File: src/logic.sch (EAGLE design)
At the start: 70 parts, among them CON1 CON-4P-TABS-JST_GH-RA, CON11 PINHEAD_1X04-2, CON12 PINHEAD_1X04-2, CON2 PINHEAD_1X04-2.54, CON3 PINHEAD_2X04-PLS-2, CON4 PINHEAD_2X03-PTH-2, CON5 PINHEAD_2X03-PTH-2, IC1 STM32F105RCT6, IC10 LM75-TSSOP8, IC11 LM75-TSSOP8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

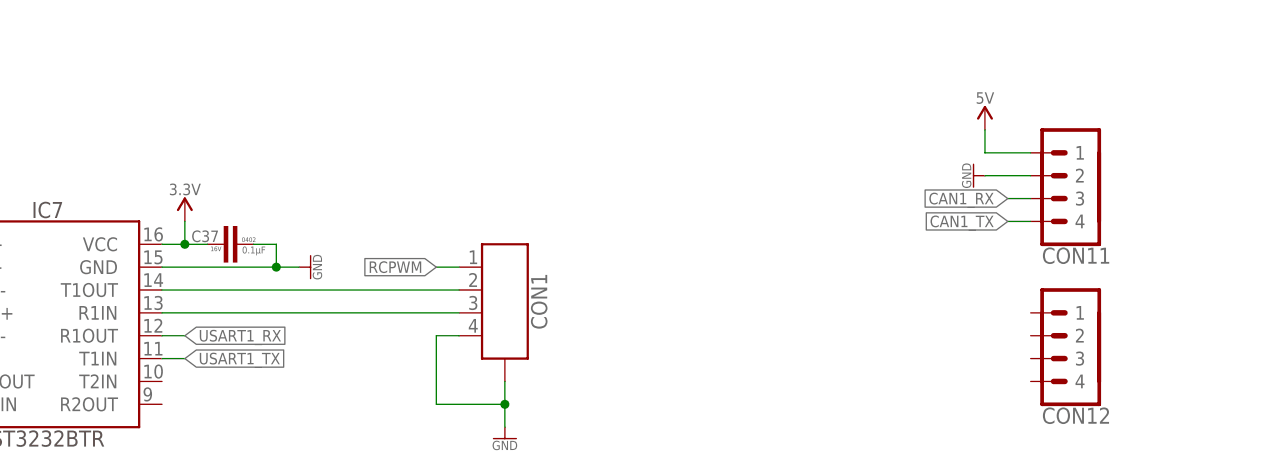
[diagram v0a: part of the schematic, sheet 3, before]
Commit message: RC PWM updated
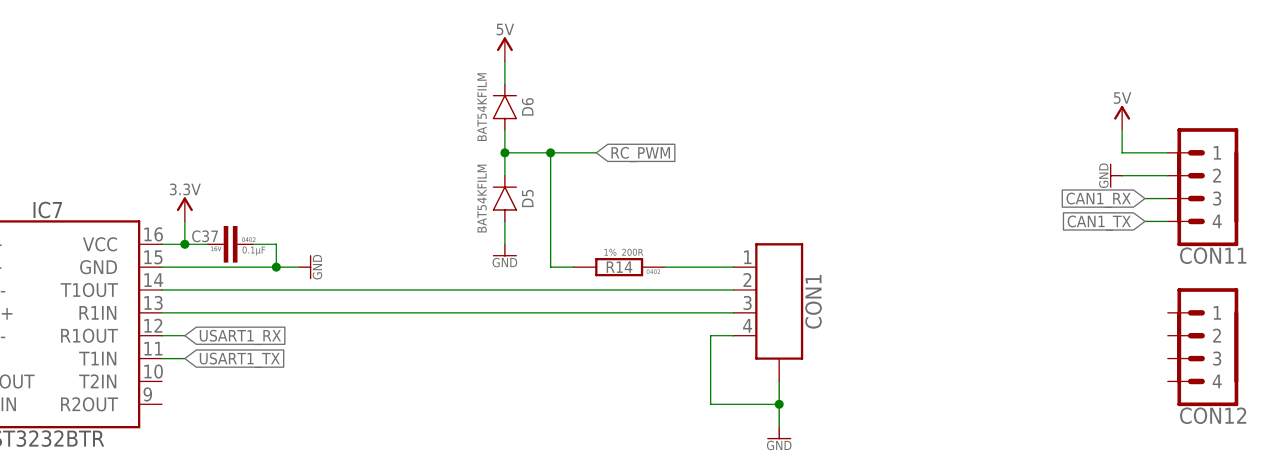
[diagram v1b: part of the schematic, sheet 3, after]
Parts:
- added D5, D6: BAT54KFILM, Diodes:BAT54KFILM
- added R14: 200R, rc:R-1%-0402
- C1, C31: value 18pF -> 9pF; AEC-Q --- -> (none); DIGIKEY# 399-8828-1-ND -> 1276-1617-1-ND; LCSC# (none) -> C111805; MANF Kemet -> Samsung Electro-Mechanics; MANF# CBR04C180F5GAC -> CL05C090DB5NNNC
- C15, C22, C25, C30: value 5600pF -> 4700pF; DIGIKEY# 1276-1579-1-ND -> 1276-1125-1-ND; LCSC# (none) -> C1538; MANF# CL05B562KB5NNNC -> CL05B472KB5NNNC
- IC2: LCSC# (none) -> C81340
- R10, R8: value 47K -> 51K; DIGIKEY# 311-47.0KCRCT-ND -> 13-RT0805FRE0751KLCT-ND; LCSC# (none) -> C25794; MANF# RC0805FR-0747KL -> RT0805FRE0751KL; OPERATING_TEMP -55°C ~ 155°C -> -55°C ~ 155°C
- R11, R15, R9: value 1K5 -> 1K8; DIGIKEY# 311-1.50KLRCT-ND -> 311-1.80KLRCT-ND; LCSC# (none) -> C25871; MANF# RC0402FR-071K5L -> RC0402FR-071K8L
- R7: value 47K -> 51K; DIGIKEY# 311-47.0KCRCT-ND -> 13-RT0805FRE0751KLCT-ND; LCSC# (none) -> C25794; MANF# RC0805FR-0747KL -> RT0805FRE0751KL
- X1: DIGIKEY# 1253-1198-1-ND -> (none); ESR (none) -> 60Ω; LOAD_CAPACITANCE (none) -> 9pF; LSCSC# (none) -> C13738; MANF (none) -> Yangxing Tech; MANF# CX3225GB24000P0HPQCC -> X322516MLB4SI
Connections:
- removed net RCPWM: CON1.1
- removed net TSENS_OS: IC1.PB4
- net GND: now also D5.A
- net N$2: now also CON1.1, R14.1
- net RC_PWM: now also D5.C, D6.A, R14.2
- net VDD_5V: now also D6.C
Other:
- note added: "Max PHASE_x voltage should be around VDC_max VDC_max = 22 * 4.2 V = 92.4 V With resistor divider formed by 51K and 1K8 resistors SENSE_x max voltage is 92.4 * (1.8/(51+1.8)) = 3.15 V"
- note removed: "Max PHASE_x voltage should be around VDC_max VDC_max = 22 * 4.2 V = 92.4 V With resistor divider formed by 47K and 1K5 resistors SENSE_x max voltage is 92.4 * (1.5/(47+1.5)) = 2.85 V"
- note removed: "Place R26 TO WRITE PROTECT"
- moved on the sheet: C1, C31, CON1, CON11, CON12

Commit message: Crystal attributes update
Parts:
- X1: DIGIKEY# (none) -> SER4372CT-ND; MANF Yangxing Tech -> EPSON; MANF# X322516MLB4SI -> TSX-3225 16.0000MF18X-AC6
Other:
- note added: "Vout = 1.225 * (10/1 + 1) ~13.5 V"
- note added: "Vout = 1.225 * (Rfb2/Rfb1 + 1)"
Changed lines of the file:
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@@
 <attribute name="MANF#" value="RC0402FR-0714KL"/>
 </part>
-<part name="RFB2" library="rc" library_urn="urn:adsk.eagle:library:2539423" deviceset="R" device="-0402" package3d_urn="urn:adsk.eagle:package:2539456/2" technology="-1%" value="3K">
-<attribute name="DIGIKEY#" value="311-3.0KJRCT-ND"/>
-<attribute name="MANF" value="Yageo"/>
-<attribute name="MANF#" value="RC0402JR-073KL"/>
+<part name="RFB2" library="rc" library_urn="urn:adsk.eagle:library:2539423" deviceset="R" device="-0402" package3d_urn="urn:adsk.eagle:package:2539456/2" technology="-1%" value="10K">
+<attribute name="DIGIKEY#" value="P10.0KLCT-ND"/>
+<attribute name="MANF" value="Panasonic Electronic Components"/>
+<attribute name="MANF#" value="ERJ-2RKF1002X"/>
 <attribute name="OPERATING_TEMP" value="-55°C ~ 155°C"/>
 </part>
@@
 1264EY-101M=P3 from Murata Electronics.
 https://www.digikey.com/en/products/detail/murata-electronics/1264EY-101M=P3/5271456</text>
+<text x="142.24" y="104.14" size="1.778" layer="97">Vout = 1.225 * (10/1 + 1) ~13.5 V</text>
+<text x="142.24" y="106.68" size="1.778" layer="97">Vout = 1.225 * (Rfb2/Rfb1 + 1)</text>
 </plain>
 <instances>
@@
 </part>
 <part name="X1" library="crystal" library_urn="urn:adsk.eagle:library:2539107" deviceset="CRYSTAL-4P" device="-3.2X2.5" package3d_urn="urn:adsk.eagle:package:2539117/3" technology="-16MHZ" value="16MHz">
-<attribute name="DIGIKEY#" value=""/>
+<attribute name="DIGIKEY#" value="SER4372CT-ND"/>
 <attribute name="ESR" value="60Ω"/>
 <attribute name="LOAD_CAPACITANCE" value="9pF"/>
 <attribute name="LSCSC#" value="C13738"/>
-<attribute name="MANF" value="Yangxing Tech"/>
-<attribute name="MANF#" value="X322516MLB4SI"/>
+<attribute name="MANF" value="EPSON"/>
+<attribute name="MANF#" value="TSX-3225 16.0000MF18X-AC6"/>
 </part>
 <part name="C6" library="rc" library_urn="urn:adsk.eagle:library:2539423" deviceset="C" device="-0402" package3d_urn="urn:adsk.eagle:package:2539461/2" value="0.1µF">

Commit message: DC-DC design notes update
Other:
- note added: "Ipeak = (Vin-Vout)/L * Ton = 0.5948670707 A"
- note added: "Ton = Vout/Vin * 420nS = 0.00000015182 S"
- note added: "Vin = 13.5V"
- note removed: "Ipeak = (Vin-Vout)/L * Ton = 0.6335127273 A"
- note removed: "Ton = Vout/Vin * 420nS = 0.0000001344 s"
- note removed: "Vin = 15.25V"
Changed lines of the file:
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@@
 </attributes>
 <variantdefs>
-<variantdef name="basic"/>
+<variantdef name="basic" current="yes"/>
 </variantdefs>
 <classes>
@@
 <sheet>
 <plain>
-<text x="120.65" y="54.61" size="1.778" layer="97" font="vector" ratio="15" align="center-left">Vout =(R14/R18+1)*0.8</text>
-<text x="120.65" y="59.69" size="1.778" layer="97" font="vector" ratio="15" align="center-left">Vin = 15.25V</text>
-<text x="120.65" y="49.53" size="1.778" layer="97" font="vector" ratio="15" align="center-left">R14 = 51K</text>
-<text x="120.65" y="44.45" size="1.778" layer="97" font="vector" ratio="15" align="center-left">R18 = 10K</text>
-<text x="120.65" y="39.37" size="1.778" layer="97" font="vector" ratio="15" align="center-left">Vout ~ 4.88V</text>
-<text x="120.65" y="34.29" size="1.778" layer="97" font="vector" ratio="15" align="center-left">Ipeak = (Vin-Vout)/L * Ton = 0.6335127273 A</text>
-<text x="120.65" y="29.21" size="1.778" layer="97" font="vector" ratio="15" align="center-left">Ton = Vout/Vin * 420nS = 0.0000001344 s</text>
+<text x="123.19" y="120.65" size="1.778" layer="97" font="vector" ratio="15" align="center-left">Vout =(R14/R18+1)*0.8</text>
+<text x="123.19" y="125.73" size="1.778" layer="97" font="vector" ratio="15" align="center-left">Vin = 13.5V</text>
+<text x="123.19" y="115.57" size="1.778" layer="97" font="vector" ratio="15" align="center-left">R14 = 51K</text>
+<text x="123.19" y="110.49" size="1.778" layer="97" font="vector" ratio="15" align="center-left">R18 = 10K</text>
+<text x="123.19" y="105.41" size="1.778" layer="97" font="vector" ratio="15" align="center-left">Vout ~ 4.88V</text>
+<text x="123.19" y="100.33" size="1.778" layer="97" font="vector" ratio="15" align="center-left">Ipeak = (Vin-Vout)/L * Ton = 0.5948670707 A</text>
+<text x="123.19" y="95.25" size="1.778" layer="97" font="vector" ratio="15" align="center-left">Ton = Vout/Vin * 420nS = 0.00000015182 S</text>
 </plain>
 <instances>
@@
 <part name="D3" library="Diodes" library_urn="urn:adsk.eagle:library:2473263" deviceset="BAT54KFILM" device="" package3d_urn="urn:adsk.eagle:package:1040205/3"/>
 <part name="+P14" library="supply_symbols" library_urn="urn:adsk.eagle:library:5017758" deviceset="3.3V" device=""/>
-<part name="CON4" library="pinhead" library_urn="urn:adsk.eagle:library:2540341" deviceset="PINHEAD_2X03" device="-PTH-2" package3d_urn="urn:adsk.eagle:package:23506356/2"/>
-<part name="CON5" library="pinhead" library_urn="urn:adsk.eagle:library:2540341" deviceset="PINHEAD_2X03" device="-PTH-2" package3d_urn="urn:adsk.eagle:package:23506356/2"/>
+<part name="CON4" library="pinhead" library_urn="urn:adsk.eagle:library:2540341" deviceset="PINHEAD_2X03" device="-PTH-2" package3d_urn="urn:adsk.eagle:package:23506356/2">
+<variant name="basic" populate="no"/>
+</part>
+<part name="CON5" library="pinhead" library_urn="urn:adsk.eagle:library:2540341" deviceset="PINHEAD_2X03" device="-PTH-2" package3d_urn="urn:adsk.eagle:package:23506356/2">
+<variant name="basic" populate="no"/>
+</part>
 <part name="GND14" library="supply_symbols" library_urn="urn:adsk.eagle:library:13097679" deviceset="GND" device="" value="GND"/>
 <part name="GND16" library="supply_symbols" library_urn="urn:adsk.eagle:library:13097679" deviceset="GND" device="" value="GND"/>

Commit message: Notes added
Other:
- note added: "- HW id set to 3 (0b0011). - Current measurement cicuitry. - Overcurrent fault signal connected to PA6. - There are three temperature sensors (all are LM75) in total. One for each phase. - Vbat voltage measurement circuitry is modified."
- note added: "Significant differences from previous SAPOG based products"
- note removed: "LED1 should be replaced with this one https://lcsc.com/product-detail/Light-Emitting-Diodes-LED_FM-B2020RGBA-HG_C108793.html/?href=jlc-SMT"
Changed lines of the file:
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@@
 </attributes>
 <variantdefs>
-<variantdef name="basic" current="yes"/>
+<variantdef name="basic"/>
 </variantdefs>
 <classes>
@@
 <part name="D6" library="Diodes" library_urn="urn:adsk.eagle:library:2473263" deviceset="BAT54KFILM" device="" package3d_urn="urn:adsk.eagle:package:1040205/3"/>
 <part name="D5" library="Diodes" library_urn="urn:adsk.eagle:library:2473263" deviceset="BAT54KFILM" device="" package3d_urn="urn:adsk.eagle:package:1040205/3"/>
+<part name="FRAME4" library="frames" library_urn="urn:adsk.eagle:library:229" deviceset="A5P-LOC" device=""/>
 </parts>
 <sheets>
+<sheet>
+<plain>
+<text x="7.62" y="154.94" size="1.778" layer="97" font="vector">- HW id set to 3 (0b0011).
+- Current measurement cicuitry.
+- Overcurrent fault signal connected to PA6.
+- There are three temperature sensors (all are LM75) in total. One for each phase.
+- Vbat voltage measurement circuitry is modified.</text>
+<text x="7.62" y="170.18" size="1.778" layer="97" font="vector" ratio="15">Significant differences from previous SAPOG based products</text>
+</plain>
+<instances>
+<instance part="FRAME4" gate="G$1" x="0" y="0" smashed="yes">
+<attribute name="DRAWING_NAME" x="87.63" y="15.367" size="2.54" layer="94"/>
+<attribute name="LAST_DATE_TIME" x="87.63" y="10.287" size="2.286" layer="94"/>
+<attribute name="SHEET" x="100.965" y="5.207" size="2.54" layer="94"/>
+</instance>
+</instances>
+<busses>
+</busses>
+<nets>
+</nets>
+</sheet>
 <sheet>
 <description>MCU</description>
@@
 <wire x1="281.94" y1="210.82" x2="281.94" y2="254" width="0.1524" layer="97" style="shortdash"/>
 <text x="337.82" y="213.36" size="2.54" layer="97" font="vector" ratio="15">PHASE sensing</text>
-<text x="132.08" y="73.66" size="1.778" layer="91">LED1 should be replaced with this one
-https://lcsc.com/product-detail/Light-Emitting-Diodes-LED_FM-B2020RGBA-HG_C108793.html/?href=jlc-SMT</text>
 <text x="142.24" y="33.02" size="1.778" layer="97">WP pin pull up is optional</text>
 <text x="106.68" y="231.14" size="1.27" layer="97" font="vector">When current_amp_out voltage exceeds comp_ref voltage

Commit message: Connectors PCB pinheaders updated
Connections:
- new net CAN2_RX: CON12.3, IC1.PB12
- new net CAN2_TX: CON12.4, IC1.PB13
- net GND: now also CON12.2
- net RC_PWM: now also CON12.1
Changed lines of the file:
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@@
 <part name="D5" library="Diodes" library_urn="urn:adsk.eagle:library:2473263" deviceset="BAT54KFILM" device="" package3d_urn="urn:adsk.eagle:package:1040205/3"/>
 <part name="FRAME4" library="frames" library_urn="urn:adsk.eagle:library:229" deviceset="A5P-LOC" device=""/>
+<part name="GND49" library="supply_symbols" library_urn="urn:adsk.eagle:library:13097679" deviceset="GND" device="" value="GND"/>
 </parts>
 <sheets>
@@
 </segment>
 </net>
+<net name="CAN2_TX" class="0">
+<segment>
+<pinref part="IC1" gate="G$1" pin="PB13"/>
+<wire x1="124.46" y1="81.28" x2="127" y2="81.28" width="0.1524" layer="91"/>
+<label x="127" y="81.28" size="1.27" layer="95" xref="yes"/>
+</segment>
+</net>
+<net name="CAN2_RX" class="0">
+<segment>
+<pinref part="IC1" gate="G$1" pin="PB12"/>
+<wire x1="124.46" y1="78.74" x2="127" y2="78.74" width="0.1524" layer="91"/>
+<label x="127" y="78.74" size="1.27" layer="95" xref="yes"/>
+</segment>
+</net>
 </nets>
 </sheet>
@@
 <attribute name="MANF#" x="134.62" y="116.84" size="1.016" layer="95" font="vector" ratio="15" rot="MR90" align="center"/>
 </instance>
+<instance part="GND49" gate="1" x="208.28" y="101.6" smashed="yes" rot="MR90">
+<attribute name="VALUE" x="206.248" y="101.6" size="1.016" layer="96" font="vector" ratio="15" rot="MR90" align="center"/>
+</instance>
 </instances>
 <busses>
@@
 <wire x1="137.16" y1="111.76" x2="137.16" y2="114.3" width="0.1524" layer="91"/>
 <pinref part="D5" gate="G$1" pin="A"/>
+</segment>
+<segment>
+<pinref part="CON12" gate="G$1" pin="2"/>
+<pinref part="GND49" gate="1" pin="GND"/>
+<wire x1="210.82" y1="101.6" x2="208.28" y2="101.6" width="0.1524" layer="91"/>
 </segment>
 </net>
@@
 <junction x="137.16" y="121.92"/>
 </segment>
+<segment>
+<pinref part="CON12" gate="G$1" pin="1"/>
+<wire x1="210.82" y1="104.14" x2="208.28" y2="104.14" width="0.1524" layer="91"/>
+<label x="208.28" y="104.14" size="1.27" layer="95" rot="R180" xref="yes"/>
+</segment>
 </net>
 <net name="USART1_RX" class="0">
@@
 </segment>
 </net>
+<net name="CAN2_TX" class="0">
+<segment>
+<pinref part="CON12" gate="G$1" pin="4"/>
+<wire x1="210.82" y1="96.52" x2="208.28" y2="96.52" width="0.1524" layer="91"/>
+<label x="208.28" y="96.52" size="1.27" layer="95" rot="R180" xref="yes"/>
+</segment>
+</net>
+<net name="CAN2_RX" class="0">
+<segment>
+<pinref part="CON12" gate="G$1" pin="3"/>
+<wire x1="210.82" y1="99.06" x2="208.28" y2="99.06" width="0.1524" layer="91"/>
+<label x="208.28" y="99.06" size="1.27" layer="95" rot="R180" xref="yes"/>
+</segment>
+</net>
